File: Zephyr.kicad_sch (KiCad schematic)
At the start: 45 parts, among them J1 Conn_02x03_Counter_Clockwise, J11 Conn_01x03, J13 Conn_01x03, J14 Conn_01x06, J15 Micro_SD_Card, Q1 MMBT3904, Q2 MMBT3904, SW4 SW_Push, U1 STM32F405RGT6, U9 W25Q128JVS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

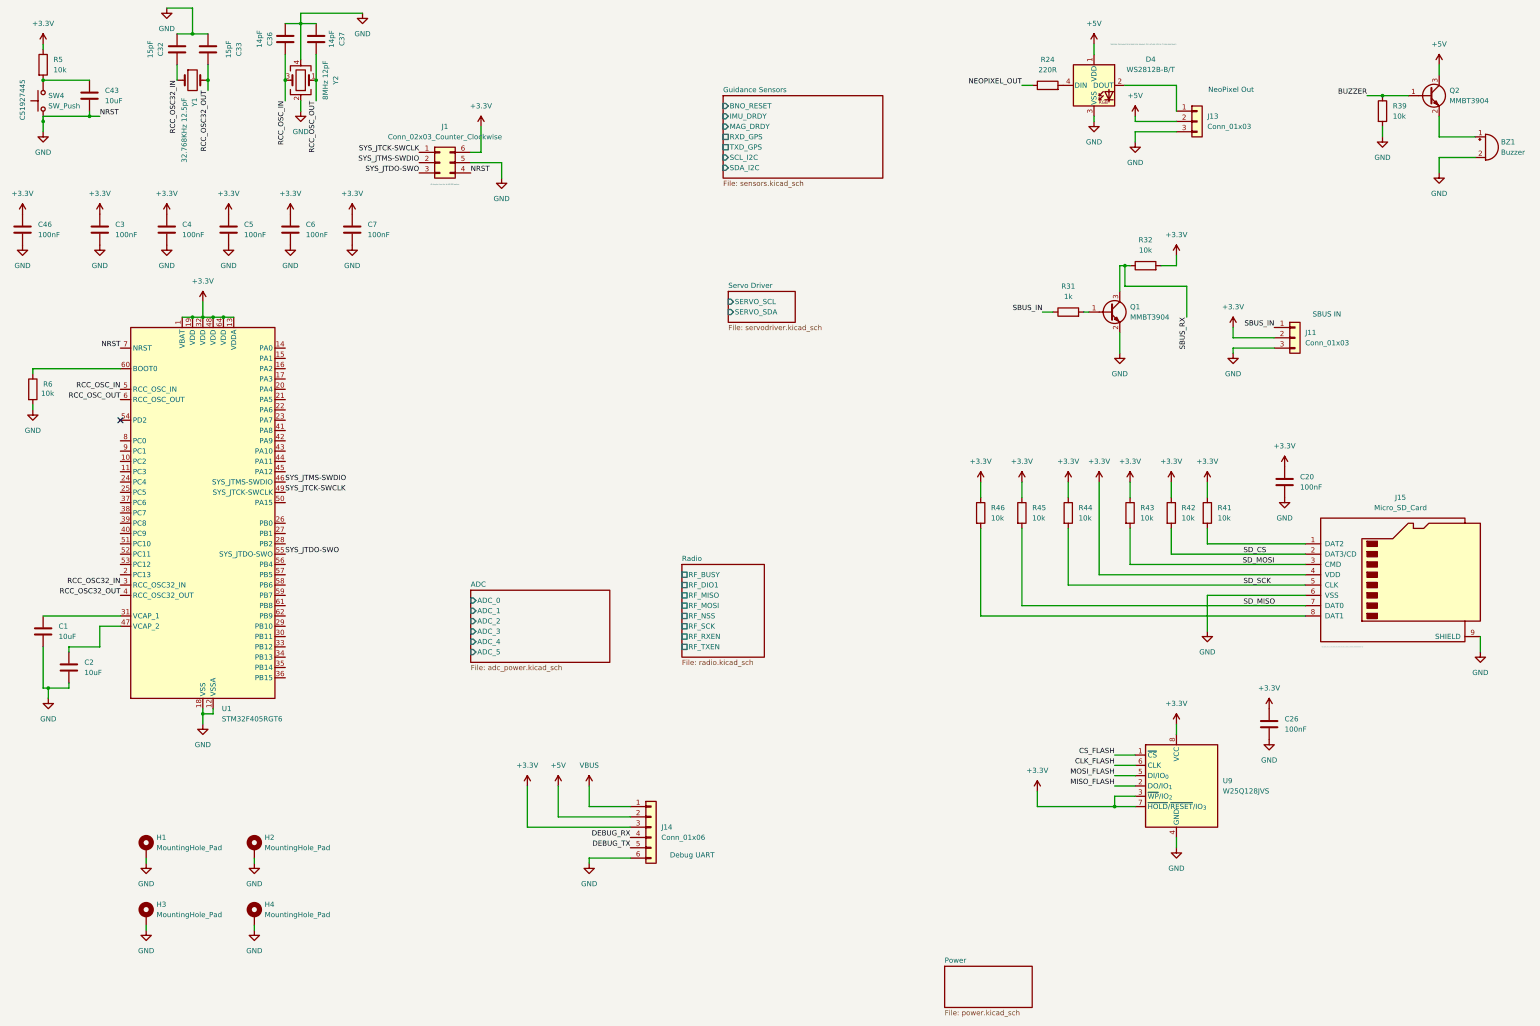
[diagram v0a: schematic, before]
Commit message: Start routing the microcontroller
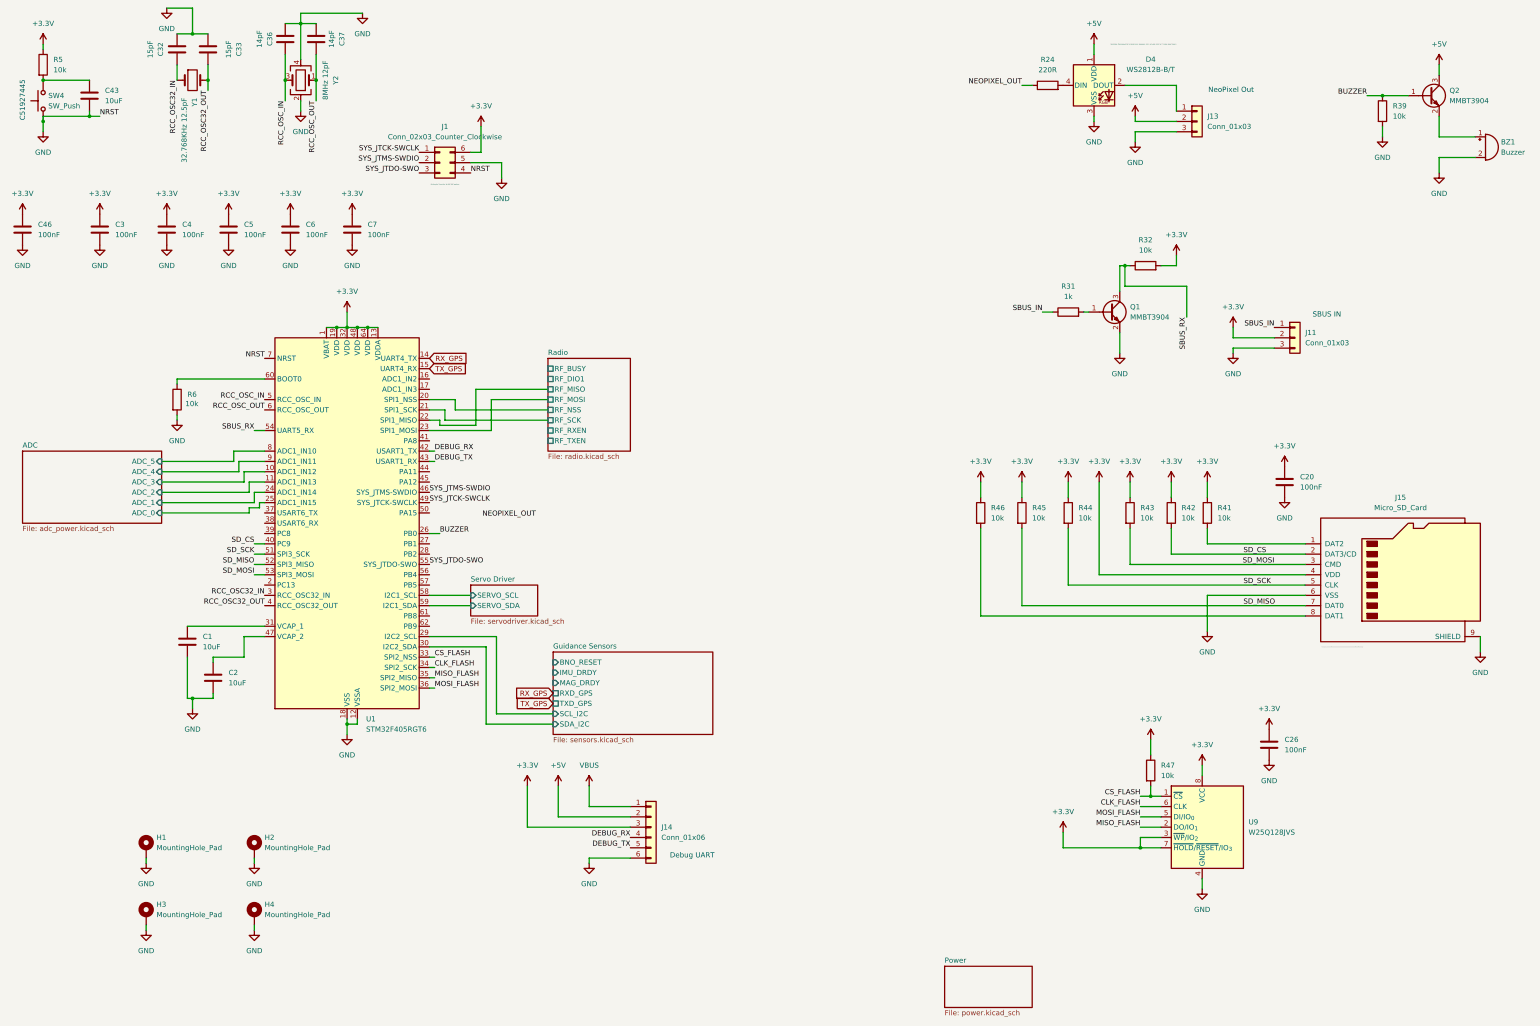
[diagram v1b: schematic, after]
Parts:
- added R47: 10k, symbol Device:R
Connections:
- net +3.3V: now also R47.1
- net ADC/ADC_0: now also U1.25 (PC5)
- net ADC/ADC_1: now also U1.24 (PC4)
- net ADC/ADC_2: now also U1.11 (PC3)
- net ADC/ADC_3: now also U1.10 (PC2)
- net ADC/ADC_4: now also U1.9 (PC1)
- net ADC/ADC_5: now also U1.8 (PC0)
- net BUZZER: now also U1.26 (PB0)
- net CLK_FLASH: now also U1.34 (PB13)
- net CS_FLASH: now also U1.33 (PB12), R47.2
- net DEBUG_RX: now also U1.42 (PA9)
- net DEBUG_TX: now also U1.43 (PA10)
- net Guidance Sensors/SCL_I2C: now also U1.29 (PB10)
- net Guidance Sensors/SDA_I2C: now also U1.30 (PB11)
- net MISO_FLASH: now also U1.35 (PB14)
- net MOSI_FLASH: now also U1.36 (PB15)
- net Radio/RF_MISO: now also U1.22 (PA6)
- net Radio/RF_MOSI: now also U1.23 (PA7)
- net Radio/RF_NSS: now also U1.20 (PA4)
- net Radio/RF_SCK: now also U1.21 (PA5)
- net SBUS_RX: now also U1.54 (PD2)
- net SD_CS: now also U1.40 (PC9)
- net SD_MISO: now also U1.52 (PC11)
- net SD_MOSI: now also U1.53 (PC12)
- net SD_SCK: now also U1.51 (PC10)
- net Servo Driver/SERVO_SCL: now also U1.58 (PB6)
- net Servo Driver/SERVO_SDA: now also U1.59 (PB7)
- net RX_GPS: now reaches U1.14 (PA0)
- net TX_GPS: now reaches U1.15 (PA1)
- no-connect marks 1 -> 0
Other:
- moved on the sheet: C1, C2, C26, R6, U1, U9

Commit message: Initial routing
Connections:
- net NEOPIXEL_OUT: now also U1.27 (PB1)
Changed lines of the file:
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@@
 	)
 	(label "NEOPIXEL_OUT"
-		(at 148.1376 139.5995 180)
+		(at 121.92 146.05 0)
 		(effects
 			(font
 				(size 1.27 1.27)
 			)
-			(justify right bottom)
+			(justify left bottom)
 		)
 	)

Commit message: Add more footprints!
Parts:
- BZ1: footprint (none) -> Buzzer_Beeper:Buzzer_12x9.5RM7.6
- C1, C2, C20, C26, C3, C32, C33, C36, C37, C4, C43, C46, C5, C6, C7: footprint Capacitor_SMD:C_0603_1608Metric_Pad1.08x0.95mm_HandSolder -> Capacitor_SMD:C_0402_1005Metric_Pad0.74x0.62mm_HandSolder
- R24, R31, R32, R39, R41, R42, R43, R44, R45, R46, R47: footprint (none) -> Resistor_SMD:R_0402_1005Metric_Pad0.72x0.64mm_HandSolder
- R5, R6: footprint Resistor_SMD:R_0603_1608Metric_Pad0.98x0.95mm_HandSolder -> Resistor_SMD:R_0402_1005Metric_Pad0.72x0.64mm_HandSolder
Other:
- sheet Radio ports: added RF_NRST; removed none
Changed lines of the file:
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@@
 			)
 		)
-		(property "Footprint" "Capacitor_SMD:C_0603_1608Metric_Pad1.08x0.95mm_HandSolder"
+		(property "Footprint" "Capacitor_SMD:C_0402_1005Metric_Pad0.74x0.62mm_HandSolder"
 			(at 39.0652 39.37 0)
 			(effects
@@
 			)
 		)
-		(property "Footprint" ""
+		(property "Footprint" "Resistor_SMD:R_0402_1005Metric_Pad0.72x0.64mm_HandSolder"
 			(at 256.032 138.43 90)
 			(effects
@@
 			)
 		)
-		(property "Footprint" "Resistor_SMD:R_0603_1608Metric_Pad0.98x0.95mm_HandSolder"
+		(property "Footprint" "Resistor_SMD:R_0402_1005Metric_Pad0.72x0.64mm_HandSolder"
 			(at 57.912 110.49 90)
 			(effects
@@
 			)
 		)
-		(property "Footprint" "Resistor_SMD:R_0603_1608Metric_Pad0.98x0.95mm_HandSolder"
+		(property "Footprint" "Resistor_SMD:R_0402_1005Metric_Pad0.72x0.64mm_HandSolder"
 			(at 24.892 27.94 90)
 			(effects
@@
 			)
 		)
-		(property "Footprint" "Capacitor_SMD:C_0603_1608Metric_Pad1.08x0.95mm_HandSolder"
+		(property "Footprint" "Capacitor_SMD:C_0402_1005Metric_Pad0.74x0.62mm_HandSolder"
 			(at 329.8952 199.39 0)
 			(effects
@@
 			)
 		)
-		(property "Footprint" ""
+		(property "Footprint" "Buzzer_Beeper:Buzzer_12x9.5RM7.6"
 			(at 381.635 45.72 90)
 			(effects
@@
 			)
 		)
-		(property "Footprint" ""
+		(property "Footprint" "Resistor_SMD:R_0402_1005Metric_Pad0.72x0.64mm_HandSolder"
 			(at 298.45 79.248 90)
 			(effects
@@
 			)
 		)
-		(property "Footprint" "Capacitor_SMD:C_0603_1608Metric_Pad1.08x0.95mm_HandSolder"
+		(property "Footprint" "Capacitor_SMD:C_0402_1005Metric_Pad0.74x0.62mm_HandSolder"
 			(at 88.5952 72.39 0)
 			(effects
@@
 			)
 		)
-		(property "Footprint" "Capacitor_SMD:C_0603_1608Metric_Pad1.08x0.95mm_HandSolder"
+		(property "Footprint" "Capacitor_SMD:C_0402_1005Metric_Pad0.74x0.62mm_HandSolder"
 			(at 333.7052 134.62 0)
 			(effects
@@
 			)
 		)
-		(property "Footprint" ""
+		(property "Footprint" "Resistor_SMD:R_0402_1005Metric_Pad0.72x0.64mm_HandSolder"
 			(at 303.022 138.43 90)
 			(effects
@@
 			)
 		)
-		(property "Footprint" ""
+		(property "Footprint" "Resistor_SMD:R_0402_1005Metric_Pad0.72x0.64mm_HandSolder"
 			(at 355.092 39.37 90)
 			(effects
@@
 			)
 		)
-		(property "Footprint" "Capacitor_SMD:C_0603_1608Metric_Pad1.08x0.95mm_HandSolder"
+		(property "Footprint" "Capacitor_SMD:C_0402_1005Metric_Pad0.74x0.62mm_HandSolder"
 			(at 22.5552 72.39 0)
 			(effects
@@
 			)
 		)
-		(property "Footprint" ""
+		(property "Footprint" "Resistor_SMD:R_0402_1005Metric_Pad0.72x0.64mm_HandSolder"
 			(at 274.32 34.798 90)
 			(effects
@@
 			)
 		)
-		(property "Footprint" "Capacitor_SMD:C_0603_1608Metric_Pad1.08x0.95mm_HandSolder"
+		(property "Footprint" "Capacitor_SMD:C_0402_1005Metric_Pad0.74x0.62mm_HandSolder"
 			(at 63.1952 173.99 0)
 			(effects
@@
 			)
 		)
-		(property "Footprint" "Capacitor_SMD:C_0603_1608Metric_Pad1.08x0.95mm_HandSolder"
+		(property "Footprint" "Capacitor_SMD:C_0402_1005Metric_Pad0.74x0.62mm_HandSolder"
 			(at 58.1152 72.39 0)
 			(effects
@@
 			)
 		)
-		(property "Footprint" "Capacitor_SMD:C_0603_1608Metric_Pad1.08x0.95mm_HandSolder"
+		(property "Footprint" "Capacitor_SMD:C_0402_1005Metric_Pad0.74x0.62mm_HandSolder"
 			(at 69.5452 182.88 0)
 			(effects
@@
 			)
 		)
-		(property "Footprint" "Capacitor_SMD:C_0603_1608Metric_Pad1.08x0.95mm_HandSolder"
+		(property "Footprint" "Capacitor_SMD:C_0402_1005Metric_Pad0.74x0.62mm_HandSolder"
 			(at 73.3552 72.39 0)
 			(effects
@@
 			)
 		)
-		(property "Footprint" ""
+		(property "Footprint" "Resistor_SMD:R_0402_1005Metric_Pad0.72x0.64mm_HandSolder"
 			(at 266.192 138.43 90)
 			(effects
@@
 			)
 		)
-		(property "Footprint" ""
+		(property "Footprint" "Resistor_SMD:R_0402_1005Metric_Pad0.72x0.64mm_HandSolder"
 			(at 297.942 201.93 90)
 			(effects
@@
 			)
 		)
-		(property "Footprint" "Capacitor_SMD:C_0603_1608Metric_Pad1.08x0.95mm_HandSolder"
+		(property "Footprint" "Capacitor_SMD:C_0402_1005Metric_Pad0.74x0.62mm_HandSolder"
 			(at 94.9452 25.4 0)
 			(effects
@@
 			)
 		)
-		(property "Footprint" "Capacitor_SMD:C_0603_1608Metric_Pad1.08x0.95mm_HandSolder"
+		(property "Footprint" "Capacitor_SMD:C_0402_1005Metric_Pad0.74x0.62mm_HandSolder"
 			(at 60.6552 27.94 0)
 			(effects
@@
 			)
 		)
-		(property "Footprint" ""
+		(property "Footprint" "Resistor_SMD:R_0402_1005Metric_Pad0.72x0.64mm_HandSolder"
 			(at 292.862 138.43 90)
 			(effects
@@
 			)
 		)
-		(property "Footprint" "Capacitor_SMD:C_0603_1608Metric_Pad1.08x0.95mm_HandSolder"
+		(property "Footprint" "Capacitor_SMD:C_0402_1005Metric_Pad0.74x0.62mm_HandSolder"
 			(at 103.8352 72.39 0)
 			(effects
@@
 			)
 		)
-		(property "Footprint" "Capacitor_SMD:C_0603_1608Metric_Pad1.08x0.95mm_HandSolder"
+		(property "Footprint" "Capacitor_SMD:C_0402_1005Metric_Pad0.74x0.62mm_HandSolder"
 			(at 87.3252 25.4 0)
 			(effects
@@
 			)
 		)
-		(property "Footprint" ""
+		(property "Footprint" "Resistor_SMD:R_0402_1005Metric_Pad0.72x0.64mm_HandSolder"
 			(at 279.4 90.678 90)
 			(effects
@@
 			)
 		)
-		(property "Footprint" "Capacitor_SMD:C_0603_1608Metric_Pad1.08x0.95mm_HandSolder"
+		(property "Footprint" "Capacitor_SMD:C_0402_1005Metric_Pad0.74x0.62mm_HandSolder"
 			(at 68.2752 27.94 0)
 			(effects
@@
 			)
 		)
-		(property "Footprint" "Capacitor_SMD:C_0603_1608Metric_Pad1.08x0.95mm_HandSolder"
+		(property "Footprint" "Capacitor_SMD:C_0402_1005Metric_Pad0.74x0.62mm_HandSolder"
 			(at 41.6052 72.39 0)
 			(effects
@@
 			)
 		)
-		(property "Footprint" ""
+		(property "Footprint" "Resistor_SMD:R_0402_1005Metric_Pad0.72x0.64mm_HandSolder"
 			(at 311.912 138.43 90)
 			(effects
@@
 			)
 		)
-		(property "Footprint" ""
+		(property "Footprint" "Resistor_SMD:R_0402_1005Metric_Pad0.72x0.64mm_HandSolder"
 			(at 277.622 138.43 90)
 			(effects
@@
 	(sheet
 		(at 151.13 100.33)
-		(size 20.32 22.86)
+		(size 20.32 25.4)
 		(exclude_from_sim no)
 		(in_bom yes)
@@
 		)
 		(property "Sheetfile" "radio.kicad_sch"
-			(at 151.13 123.7746 0)
+			(at 151.13 126.3146 0)
 			(effects
 				(font
@@
 			(effects
 				(font
+					(size 1.27 1.27)
+				)
+				(justify left)
+			)
+		)
+		(pin "RF_NRST" passive
+			(at 151.13 123.19 180)
+			(effects
+				(font

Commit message: Reset circuit fix (oops...)
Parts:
- added C29: 1uF, Capacitor_SMD:C_0402_1005Metric_Pad0.74x0.62mm_HandSolder, symbol Device:C
- added C30: 10uF, Capacitor_SMD:C_0402_1005Metric_Pad0.74x0.62mm_HandSolder, symbol Device:C
- C43: value 10uF -> 100nF
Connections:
- net +3.3V: now also C29.1, C30.1
- net GND: now also C29.2, C30.2; no longer J1.4 (Pin_4), U1.7 (NRST)
- net NRST: now reaches C43.1, R5.2, SW4.2
- net NRST: now also J1.4 (Pin_4), U1.7 (NRST)
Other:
- title: (none) -> Zephyr Flight Computer
- moved on the sheet: C20

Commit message: Continue work
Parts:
- added D7: SS14, Diode_SMD:D_SMA, symbol Diode:SS14
- added R12: 10k, Resistor_SMD:R_0402_1005Metric_Pad0.72x0.64mm_HandSolder, symbol Device:R
- J11, J13: footprint (none) -> Connector_PinHeader_2.54mm:PinHeader_1x03_P2.54mm_Vertical
- J14: footprint (none) -> Connector_PinHeader_2.54mm:PinHeader_1x06_P2.54mm_Vertical
- J15: footprint (none) -> lcsc:TF-SMD_HX-TF-CARD-H1.8-SY
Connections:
- net +3.3V: now also R12.1
- net +5V: now also D7.2 (A); no longer D4.1 (VDD)
- net GND: now also J15.10 (SHIELD); no longer J15.9 (SHIELD)
- net CD: now reaches U1.39 (PC8)
- net CD: now also J15.9 (CD), R12.2
- new net: D4.1 (VDD), D7.1 (K)
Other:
- note added: "C19189036"
- note added: "C96093"
- note removed: "Normally, there would be a diode here. However, 5V is actually 4.2V so it's okay (see Power)"
- moved on the sheet: D4, J13, R24

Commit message: Start PCB layout
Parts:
- SW4: footprint libsos41:SMD_SW_NEW_REDONE -> lcsc:SW-SMD_4P-L3.5-W3.0-P1.50-LS4.7
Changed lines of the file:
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@@
 			)
 		)
-		(property "Footprint" "libsos41:SMD_SW_NEW_REDONE"
+		(property "Footprint" "lcsc:SW-SMD_4P-L3.5-W3.0-P1.50-LS4.7"
 			(at 21.59 36.83 0)
 			(effects

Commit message: Start layout
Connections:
- net Guidance Sensors/BNO_RESET: now also U1.62 (PB9)
- net SYS_JTCK-SWCLK: now also J1.2 (Pin_2); no longer J1.1 (Pin_1)
- net SYS_JTMS-SWDIO: now also J1.1 (Pin_1); no longer J1.2 (Pin_2)
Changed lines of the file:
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@@
+	(wire
+		(pts
+			(xy 152.4 175.26) (xy 144.78 175.26)
+		)
+		(stroke
+			(width 0)
+			(type default)
+		)
+	)
 	(wire
 		(pts
@@
 	(wire
 		(pts
+			(xy 144.78 175.26) (xy 144.78 166.37)
+		)
+		(stroke
+			(width 0)
+			(type default)
+		)
+	)
+	(wire
+		(pts
 			(xy 283.21 88.9) (xy 284.48 88.9)
 		)
@@
 		(pts
 			(xy 320.04 95.25) (xy 330.2 95.25)
+		)
+		(stroke
+			(width 0)
+			(type default)
+		)
+	)
+	(wire
+		(pts
+			(xy 144.78 166.37) (xy 121.92 166.37)
 		)
 		(stroke
@@
 		)
 	)
-	(label "SYS_JTMS-SWDIO"
-		(at 119.38 52.07 180)
-		(effects
-			(font
-				(size 1.27 1.27)
-			)
-			(justify right bottom)
-		)
-	)
 	(label "RCC_OSC32_OUT"
 		(at 67.31 34.29 270)
@@
 		)
 	)
+	(label "SYS_JTMS-SWDIO"
+		(at 119.38 49.53 180)
+		(effects
+			(font
+				(size 1.27 1.27)
+			)
+			(justify right bottom)
+		)
+	)
 	(label "SBUS_IN"
 		(at 330.2 92.71 180)
@@
 		)
 	)
-	(label "SYS_JTCK-SWCLK"
-		(at 119.38 49.53 180)
-		(effects
-			(font
-				(size 1.27 1.27)
-			)
-			(justify right bottom)
-		)
-	)
 	(label "CS_FLASH"
 		(at 297.18 208.28 180)
@@
 		(effects
 			(font
+				(size 1.27 1.27)
+			)
+			(justify right bottom)
+		)
+	)
+	(label "SYS_JTCK-SWCLK"
+		(at 119.38 52.07 180)
+		(effects
+			(font
